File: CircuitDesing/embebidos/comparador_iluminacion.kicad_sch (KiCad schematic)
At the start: 5 parts

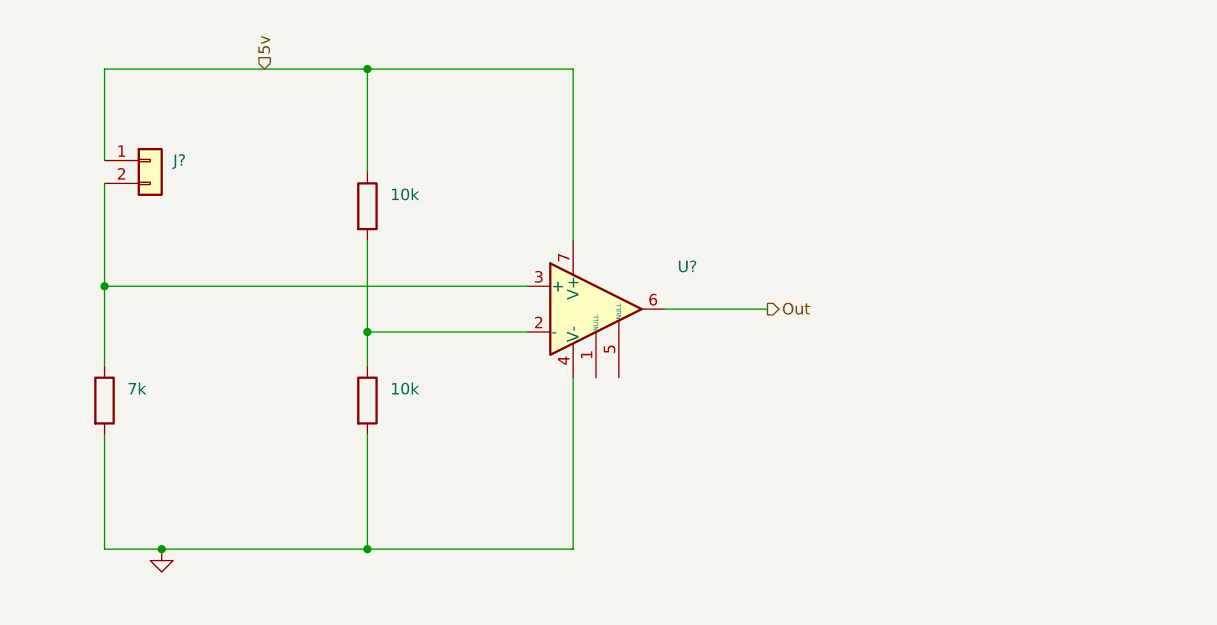
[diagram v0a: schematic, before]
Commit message: Sensor Ultrasonido
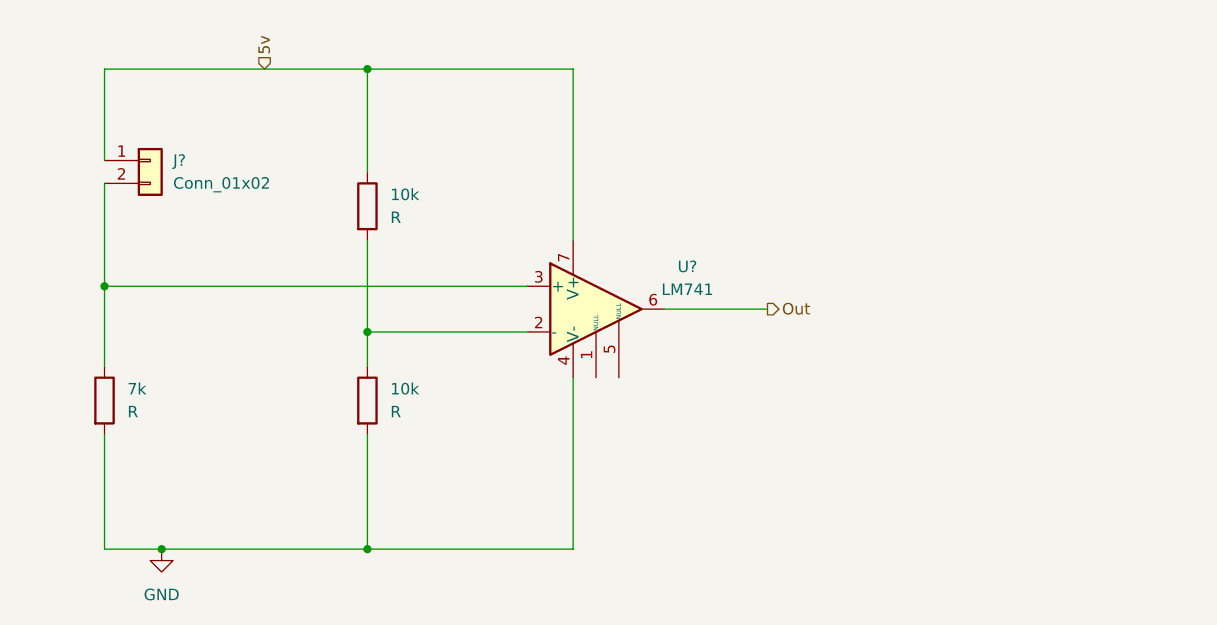
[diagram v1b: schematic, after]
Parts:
- 10k, 7k: value (none) -> R
- J?: value (none) -> Conn_01x02
- U?: value (none) -> LM741
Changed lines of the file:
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@@
       (effects (font (size 1.27 1.27)) hide)
     )
-    (property "Value" "" (id 1) (at 81.28 107.95 0))
+    (property "Value" "GND" (id 1) (at 81.28 107.95 0))
     (property "Footprint" "" (id 2) (at 81.28 102.87 0)
       (effects (font (size 1.27 1.27)) hide)
@@
       (effects (font (size 1.27 1.27)) (justify left))
     )
-    (property "Value" "" (id 1) (at 82.55 62.23 0)
+    (property "Value" "Conn_01x02" (id 1) (at 82.55 62.23 0)
       (effects (font (size 1.27 1.27)) (justify left))
     )
@@
       (effects (font (size 1.27 1.27)) (justify left))
     )
-    (property "Value" "" (id 1) (at 106.68 87.6299 0)
+    (property "Value" "R" (id 1) (at 106.68 87.6299 0)
       (effects (font (size 1.27 1.27)) (justify left))
     )
@@
       (effects (font (size 1.27 1.27)) (justify left))
     )
-    (property "Value" "" (id 1) (at 77.47 87.6299 0)
+    (property "Value" "R" (id 1) (at 77.47 87.6299 0)
       (effects (font (size 1.27 1.27)) (justify left))
     )
@@
     (in_bom yes) (on_board yes) (fields_autoplaced)
     (property "Reference" "U?" (id 0) (at 139.7 71.501 0))
-    (property "Value" "" (id 1) (at 139.7 74.041 0))
+    (property "Value" "LM741" (id 1) (at 139.7 74.041 0))
     (property "Footprint" "" (id 2) (at 130.81 74.93 0)
       (effects (font (size 1.27 1.27)) hide)
@@
       (effects (font (size 1.27 1.27)) (justify left))
     )
-    (property "Value" "" (id 1) (at 106.68 66.0399 0)
+    (property "Value" "R" (id 1) (at 106.68 66.0399 0)
       (effects (font (size 1.27 1.27)) (justify left))
     )

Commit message: Huellas parciales
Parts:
- 10k1, 10k2: renamed from 10k; footprint (none) -> Resistor_SMD:R_0603_1608Metric_Pad0.98x0.95mm_HandSolder
- 7k1: renamed from 7k; footprint (none) -> Resistor_SMD:R_0603_1608Metric_Pad0.98x0.95mm_HandSolder
- gave numbers to parts that had none: 2
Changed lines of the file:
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@@
   (symbol (lib_id "power:GND") (at 81.28 102.87 0) (unit 1)
     (in_bom yes) (on_board yes) (fields_autoplaced)
-    (property "Reference" "#PWR?" (id 0) (at 81.28 109.22 0)
+    (property "Reference" "#PWR024" (id 0) (at 81.28 109.22 0)
       (effects (font (size 1.27 1.27)) hide)
     )
@@
   (symbol (lib_id "Connector_Generic:Conn_01x02") (at 80.01 59.69 0) (unit 1)
     (in_bom yes) (on_board yes)
-    (property "Reference" "J?" (id 0) (at 82.55 59.6899 0)
+    (property "Reference" "J1" (id 0) (at 82.55 59.6899 0)
       (effects (font (size 1.27 1.27)) (justify left))
     )
@@
   (symbol (lib_id "Device:R") (at 104.14 86.36 0) (unit 1)
     (in_bom yes) (on_board yes) (fields_autoplaced)
-    (property "Reference" "10k" (id 0) (at 106.68 85.0899 0)
+    (property "Reference" "10k2" (id 0) (at 106.68 85.0899 0)
       (effects (font (size 1.27 1.27)) (justify left))
     )
@@
       (effects (font (size 1.27 1.27)) (justify left))
     )
-    (property "Footprint" "" (id 2) (at 102.362 86.36 90)
+    (property "Footprint" "Resistor_SMD:R_0603_1608Metric_Pad0.98x0.95mm_HandSolder" (id 2) (at 102.362 86.36 90)
       (effects (font (size 1.27 1.27)) hide)
     )
@@
   (symbol (lib_id "Device:R") (at 74.93 86.36 0) (unit 1)
     (in_bom yes) (on_board yes) (fields_autoplaced)
-    (property "Reference" "7k" (id 0) (at 77.47 85.0899 0)
+    (property "Reference" "7k1" (id 0) (at 77.47 85.0899 0)
       (effects (font (size 1.27 1.27)) (justify left))
     )
@@
       (effects (font (size 1.27 1.27)) (justify left))
     )
-    (property "Footprint" "" (id 2) (at 73.152 86.36 90)
+    (property "Footprint" "Resistor_SMD:R_0603_1608Metric_Pad0.98x0.95mm_HandSolder" (id 2) (at 73.152 86.36 90)
       (effects (font (size 1.27 1.27)) hide)
     )
@@
   (symbol (lib_id "Amplifier_Operational:LM741") (at 129.54 76.2 0) (unit 1)
     (in_bom yes) (on_board yes) (fields_autoplaced)
-    (property "Reference" "U?" (id 0) (at 139.7 71.501 0))
+    (property "Reference" "U4" (id 0) (at 139.7 71.501 0))
     (property "Value" "LM741" (id 1) (at 139.7 74.041 0))
     (property "Footprint" "" (id 2) (at 130.81 74.93 0)
@@
   (symbol (lib_id "Device:R") (at 104.14 64.77 0) (unit 1)
     (in_bom yes) (on_board yes) (fields_autoplaced)
-    (property "Reference" "10k" (id 0) (at 106.68 63.4999 0)
+    (property "Reference" "10k1" (id 0) (at 106.68 63.4999 0)
       (effects (font (size 1.27 1.27)) (justify left))
     )
@@
       (effects (font (size 1.27 1.27)) (justify left))
     )
-    (property "Footprint" "" (id 2) (at 102.362 64.77 90)
+    (property "Footprint" "Resistor_SMD:R_0603_1608Metric_Pad0.98x0.95mm_HandSolder" (id 2) (at 102.362 64.77 90)
       (effects (font (size 1.27 1.27)) hide)
     )

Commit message: Todas las huellas
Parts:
- J1: footprint (none) -> Connector_JST:JST_EH_B2B-EH-A_1x02_P2.50mm_Vertical
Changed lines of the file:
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@@
       (effects (font (size 1.27 1.27)) (justify left))
     )
-    (property "Footprint" "" (id 2) (at 80.01 59.69 0)
+    (property "Footprint" "Connector_JST:JST_EH_B2B-EH-A_1x02_P2.50mm_Vertical" (id 2) (at 80.01 59.69 0)
       (effects (font (size 1.27 1.27)) hide)
     )

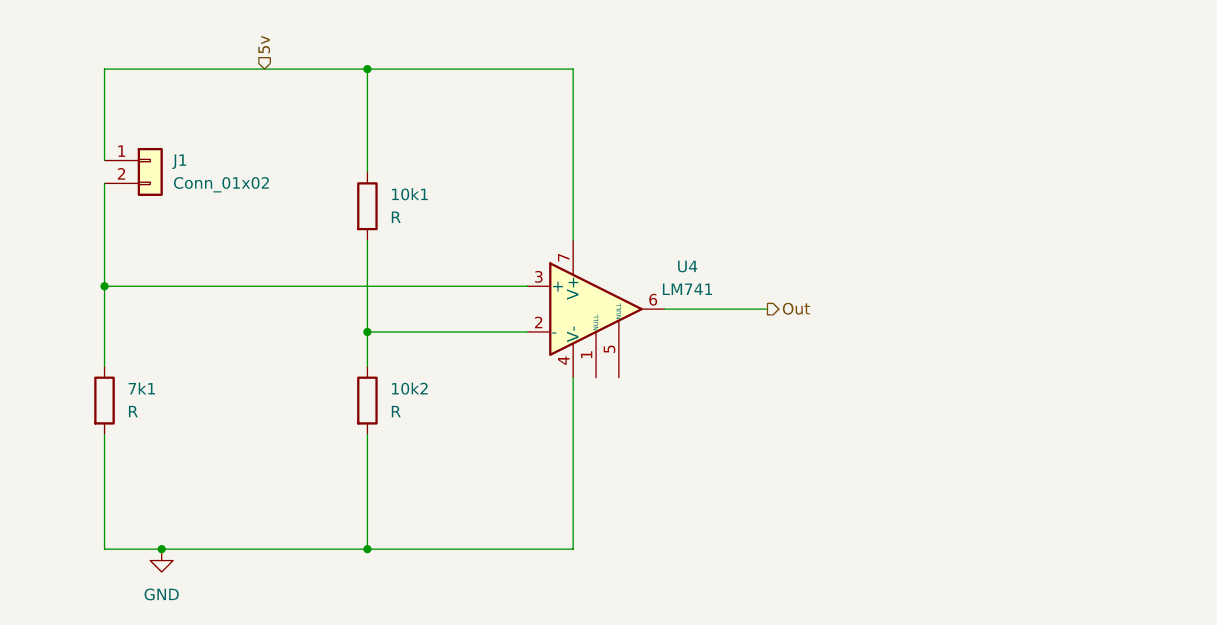
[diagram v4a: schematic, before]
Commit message: pull up
Circuito LDR
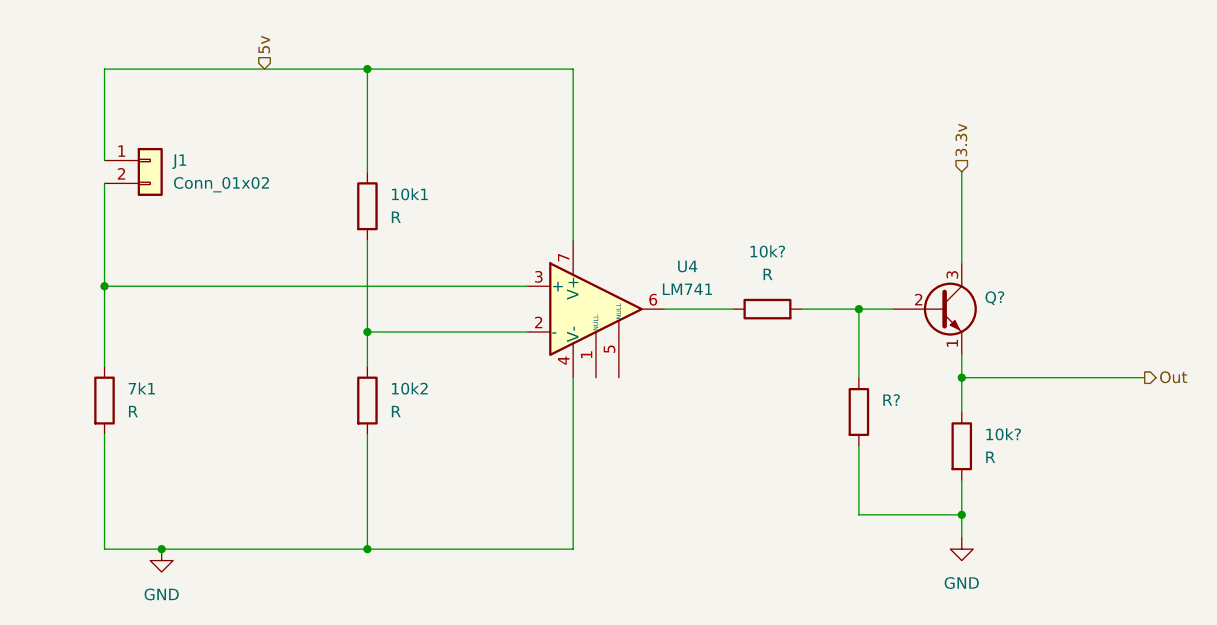
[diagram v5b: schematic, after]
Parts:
- added 10k? (x2): R, Resistor_SMD:R_0603_1608Metric_Pad0.98x0.95mm_HandSolder, symbol Device:R
- added Q?: (no value), symbol Transistor_BJT:2N2219
- added R?: (no value), symbol Device:R
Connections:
- net GND: now also 10k?.2, R?.2
- net Out: now also 10k?.1, Q?.1 (E); no longer U4.6
- new net: 10k?.1, U4.6
- new net: 10k?.2, Q?.2 (B), R?.1
- new net 3.3v: Q?.3 (C)
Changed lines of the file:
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@@
 (kicad_sch (version 20211123) (generator eeschema)
   (paper "A4")
+  (junction (at 170.18 99.06) (diameter 0) (color 0 0 0 0)
+  )
   (junction (at 74.93 73.66) (diameter 0) (color 0 0 0 0)
   )
@@
   (junction (at 104.14 49.53) (diameter 0) (color 0 0 0 0)
   )
+  (junction (at 170.18 83.82) (diameter 0) (color 0 0 0 0)
+  )
   (junction (at 104.14 102.87) (diameter 0) (color 0 0 0 0)
   )
+  (junction (at 158.75 76.2) (diameter 0) (color 0 0 0 0)
+  )
   (junction (at 81.28 102.87) (diameter 0) (color 0 0 0 0)
   )
+  (wire (pts (xy 170.18 81.28) (xy 170.18 83.82))
+    (stroke (width 0) (type default) (color 0 0 0 0))
+  )
   (wire (pts (xy 127 83.82) (xy 127 102.87))
     (stroke (width 0) (type default) (color 0 0 0 0))
@@
     (stroke (width 0) (type default) (color 0 0 0 0))
   )
+  (wire (pts (xy 170.18 83.82) (xy 190.5 83.82))
+    (stroke (width 0) (type default) (color 0 0 0 0))
+  )
   (wire (pts (xy 104.14 49.53) (xy 127 49.53))
     (stroke (width 0) (type default) (color 0 0 0 0))
@@
     (stroke (width 0) (type default) (color 0 0 0 0))
   )
+  (wire (pts (xy 170.18 99.06) (xy 170.18 101.6))
+    (stroke (width 0) (type default) (color 0 0 0 0))
+  )
   (wire (pts (xy 104.14 78.74) (xy 104.14 82.55))
     (stroke (width 0) (type default) (color 0 0 0 0))
@@
     (stroke (width 0) (type default) (color 0 0 0 0))
   )
-  (wire (pts (xy 137.16 76.2) (xy 148.59 76.2))
+  (wire (pts (xy 137.16 76.2) (xy 144.78 76.2))
+    (stroke (width 0) (type default) (color 0 0 0 0))
+  )
+  (wire (pts (xy 170.18 95.25) (xy 170.18 99.06))
     (stroke (width 0) (type default) (color 0 0 0 0))
   )
@@
     (stroke (width 0) (type default) (color 0 0 0 0))
   )
+  (wire (pts (xy 152.4 76.2) (xy 158.75 76.2))
+    (stroke (width 0) (type default) (color 0 0 0 0))
+  )
   (wire (pts (xy 127 102.87) (xy 104.14 102.87))
     (stroke (width 0) (type default) (color 0 0 0 0))
   )
+  (wire (pts (xy 158.75 91.44) (xy 158.75 99.06))
+    (stroke (width 0) (type default) (color 0 0 0 0))
+  )
+  (wire (pts (xy 158.75 76.2) (xy 158.75 83.82))
+    (stroke (width 0) (type default) (color 0 0 0 0))
+  )
+  (wire (pts (xy 158.75 76.2) (xy 162.56 76.2))
+    (stroke (width 0) (type default) (color 0 0 0 0))
+  )
+  (wire (pts (xy 170.18 83.82) (xy 170.18 87.63))
+    (stroke (width 0) (type default) (color 0 0 0 0))
+  )
   (wire (pts (xy 127 49.53) (xy 127 68.58))
     (stroke (width 0) (type default) (color 0 0 0 0))
@@
     (stroke (width 0) (type default) (color 0 0 0 0))
   )
-  (hierarchical_label "Out" (shape output) (at 148.59 76.2 0)
+  (wire (pts (xy 170.18 60.96) (xy 170.18 71.12))
+    (stroke (width 0) (type default) (color 0 0 0 0))
+  )
+  (wire (pts (xy 158.75 99.06) (xy 170.18 99.06))
+    (stroke (width 0) (type default) (color 0 0 0 0))
+  )
+  (hierarchical_label "Out" (shape output) (at 190.5 83.82 0)
     (effects (font (size 1.27 1.27)) (justify left))
   )
   (hierarchical_label "5v" (shape input) (at 92.71 49.53 90)
     (effects (font (size 1.27 1.27)) (justify left))
+  )
+  (hierarchical_label "3.3v" (shape input) (at 170.18 60.96 90)
+    (effects (font (size 1.27 1.27)) (justify left))
+  )
+  (symbol (lib_id "power:GND") (at 170.18 101.6 0) (unit 1)
+    (in_bom yes) (on_board yes) (fields_autoplaced)
+    (property "Reference" "#PWR?" (id 0) (at 170.18 107.95 0)
+      (effects (font (size 1.27 1.27)) hide)
+    )
+    (property "Value" "GND" (id 1) (at 170.18 106.68 0))
+    (property "Footprint" "" (id 2) (at 170.18 101.6 0)
+      (effects (font (size 1.27 1.27)) hide)
+    )
+    (property "Datasheet" "" (id 3) (at 170.18 101.6 0)
+      (effects (font (size 1.27 1.27)) hide)
+    )
+    (pin "1")
   )
   (symbol (lib_id "power:GND") (at 81.28 102.87 0) (unit 1)
@@
     )
     (property "Datasheet" "~" (id 3) (at 104.14 86.36 0)
+      (effects (font (size 1.27 1.27)) hide)
+    )
+    (pin "1")
+    (pin "2")
+  )
+  (symbol (lib_id "Device:R") (at 148.59 76.2 90) (unit 1)
+    (in_bom yes) (on_board yes) (fields_autoplaced)
+    (property "Reference" "10k?" (id 0) (at 148.59 69.85 90))
+    (property "Value" "R" (id 1) (at 148.59 72.39 90))
+    (property "Footprint" "Resistor_SMD:R_0603_1608Metric_Pad0.98x0.95mm_HandSolder" (id 2) (at 148.59 77.978 90)
+      (effects (font (size 1.27 1.27)) hide)
+    )
+    (property "Datasheet" "~" (id 3) (at 148.59 76.2 0)
+      (effects (font (size 1.27 1.27)) hide)
+    )
+    (pin "1")
+    (pin "2")
+  )
+  (symbol (lib_id "Device:R") (at 158.75 87.63 0) (unit 1)
+    (in_bom yes) (on_board yes) (fields_autoplaced)
+    (property "Reference" "R?" (id 0) (at 161.29 86.3599 0)
+      (effects (font (size 1.27 1.27)) (justify left))
+    )
+    (property "Value" "" (id 1) (at 161.29 88.8999 0)
+      (effects (font (size 1.27 1.27)) (justify left))
+    )
+    (property "Footprint" "" (id 2) (at 156.972 87.63 90)
+      (effects (font (size 1.27 1.27)) hide)
+    )
+    (property "Datasheet" "~" (id 3) (at 158.75 87.63 0)
       (effects (font (size 1.27 1.27)) hide)
     )
@@
     (pin "8")
   )
+  (symbol (lib_id "Transistor_BJT:2N2219") (at 167.64 76.2 0) (unit 1)
+    (in_bom yes) (on_board yes) (fields_autoplaced)
+    (property "Reference" "Q?" (id 0) (at 172.72 74.9299 0)
+      (effects (font (size 1.27 1.27)) (justify left))
+    )
+    (property "Value" "" (id 1) (at 172.72 77.4699 0)
+      (effects (font (size 1.27 1.27)) (justify left))
+    )
+    (property "Footprint" "" (id 2) (at 172.72 78.105 0)
+      (effects (font (size 1.27 1.27) italic) (justify left) hide)
+    )
+    (property "Datasheet" "http://www.onsemi.com/pub_link/Collateral/2N2219-D.PDF" (id 3) (at 167.64 76.2 0)
+      (effects (font (size 1.27 1.27)) (justify left) hide)
+    )
+    (pin "1")
+    (pin "2")
+    (pin "3")
+  )
   (symbol (lib_id "Device:R") (at 104.14 64.77 0) (unit 1)
     (in_bom yes) (on_board yes) (fields_autoplaced)
@@
       (effects (font (size 1.27 1.27)) hide)
     )
+    (pin "1")
+    (pin "2")
+  )
+  (symbol (lib_id "Device:R") (at 170.18 91.44 0) (unit 1)
+    (in_bom yes) (on_board yes) (fields_autoplaced)
+    (property "Reference" "10k?" (id 0) (at 172.72 90.1699 0)
+      (effects (font (size 1.27 1.27)) (justify left))
+    )
+    (property "Value" "R" (id 1) (at 172.72 92.7099 0)
+      (effects (font (size 1.27 1.27)) (justify left))
+    )
+    (property "Footprint" "Resistor_SMD:R_0603_1608Metric_Pad0.98x0.95mm_HandSolder" (id 2) (at 168.402 91.44 90)
+      (effects (font (size 1.27 1.27)) hide)
+    )
+    (property "Datasheet" "~" (id 3) (at 170.18 91.44 0)
+      (effects (font (size 1.27 1.27)) hide)
+    )

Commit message: Actualizacion huellas
Huellas+Programador
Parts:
- removed Q?: (no value), symbol Transistor_BJT:2N2219
- removed R?: (no value), symbol Device:R
- removed U4: LM741, symbol Amplifier_Operational:LM741
- added Q4: MMBT3904, Package_TO_SOT_SMD:SOT-23, symbol Transistor_BJT:MMBT3904
- added U3: LM4250, Package_DFN_QFN:DFN-8-1EP_2x2mm_P0.5mm_EP1.05x1.75mm, symbol Amplifier_Operational:LM4250
- gave numbers to parts that had none: 2
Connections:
- net 3.3v: now also Q4.3 (C)
- net 5v: now also U3.8 (IQ)
- net GND: now also U3.4 (V-)
- net Out: now also Q4.2 (E)
- net at 7k1.1, J1.2 (Pin_2): now also U3.3 (+)
- net at 10k1.2, 10k2.1: now also U3.2 (-)
- net at 10k3.1: now also U3.1 (NULL)
- net at 10k3.2: now also Q4.1 (B)
- no-connect marks 0 -> 3
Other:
- moved on the sheet: 10k3, 10k4

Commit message: Ruteo completo
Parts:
- U3: footprint Package_DFN_QFN:DFN-8-1EP_2x2mm_P0.5mm_EP1.05x1.75mm -> Package_DIP:DIP-8_W7.62mm_SMDSocket_SmallPads
- renumbered J1 to J3, Q4 to Q8
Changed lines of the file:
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@@
   (symbol (lib_id "power:GND") (at 160.02 91.44 0) (unit 1)
     (in_bom yes) (on_board yes) (fields_autoplaced)
-    (property "Reference" "#PWR0109" (id 0) (at 160.02 97.79 0)
+    (property "Reference" "#PWR033" (id 0) (at 160.02 97.79 0)
       (effects (font (size 1.27 1.27)) hide)
     )
@@
   (symbol (lib_id "power:GND") (at 81.28 102.87 0) (unit 1)
     (in_bom yes) (on_board yes) (fields_autoplaced)
-    (property "Reference" "#PWR024" (id 0) (at 81.28 109.22 0)
+    (property "Reference" "#PWR032" (id 0) (at 81.28 109.22 0)
       (effects (font (size 1.27 1.27)) hide)
     )
@@
   (symbol (lib_id "Connector_Generic:Conn_01x02") (at 80.01 59.69 0) (unit 1)
     (in_bom yes) (on_board yes)
-    (property "Reference" "J1" (id 0) (at 82.55 59.6899 0)
+    (property "Reference" "J3" (id 0) (at 82.55 59.6899 0)
       (effects (font (size 1.27 1.27)) (justify left))
     )
@@
     (property "Reference" "U3" (id 0) (at 139.7 71.501 0))
     (property "Value" "LM4250" (id 1) (at 139.7 74.041 0))
-    (property "Footprint" "Package_DFN_QFN:DFN-8-1EP_2x2mm_P0.5mm_EP1.05x1.75mm" (id 2) (at 130.81 74.93 0)
+    (property "Footprint" "Package_DIP:DIP-8_W7.62mm_SMDSocket_SmallPads" (id 2) (at 130.81 74.93 0)
       (effects (font (size 1.27 1.27)) hide)
     )
@@
   (symbol (lib_id "Transistor_BJT:MMBT3904") (at 157.48 66.04 0) (unit 1)
     (in_bom yes) (on_board yes) (fields_autoplaced)
-    (property "Reference" "Q4" (id 0) (at 162.56 64.7699 0)
+    (property "Reference" "Q8" (id 0) (at 162.56 64.7699 0)
       (effects (font (size 1.27 1.27)) (justify left))
     )
